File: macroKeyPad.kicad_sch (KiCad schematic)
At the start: 0 parts

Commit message: added libraries
Almost done, gotta add graphic and possibly change the thing for the kb2040
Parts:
- added D1, D2, D3, D4, D5, D6, D7, D8: Diode, ScottoKeebs_Components:Diode_SOD-123, symbol ScottoKeebs:Placeholder_Diode
- added S1, S2, S3, S4, S5, S6, S7, S8: Keyswitch, PCM_Switch_Keyboard_Kailh:SW_Kailh_Choc_V1, symbol ScottoKeebs:Placeholder_Keyswitch
- added U1: kb2040, ScottoKeebs_MCU:Adafruit_KB2040_SMD, symbol kb2040_kicad:kb2040
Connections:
- new net: D5.2 (A), S5.2
- new net: D4.2 (A), S4.2
- new net: D1.2 (A), S1.2
- new net: D6.2 (A), S6.2
- new net: D2.2 (A), S2.2
- new net: D3.2 (A), S3.2
- new net: D8.2 (A), S8.2
- new net: D7.2 (A), S7.2
- new net Col0: S1.1, S5.1, U1.19 (A3/29)
- new net Col1: S2.1, S6.1, U1.20 (A2/28)
- new net Col2: S3.1, S7.1, U1.21 (A1/27)
- new net Col3: S4.1, S8.1, U1.22 (A0/26)
- new net Row0: D1.1 (K), D2.1 (K), D3.1 (K), D4.1 (K), U1.23 (SCK/18)
- new net Row1: D5.1 (K), D6.1 (K), D7.1 (K), D8.1 (K), U1.24 (MISO/20)

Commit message: pretty close to being done
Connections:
- net Col0: now also U1.11 (D7); no longer U1.19 (A3/29)
- net Col1: now also U1.10 (D6); no longer U1.20 (A2/28)
- net Col2: now also U1.9 (D5); no longer U1.21 (A1/27)
- net Col3: now also U1.8 (D4); no longer U1.22 (A0/26)
- net Row0: now also U1.7 (D3); no longer U1.23 (SCK/18)
- net Row1: now also U1.6 (D2); no longer U1.24 (MISO/20)

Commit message: wiring
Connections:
- net Col0: no longer U1.11 (D7)
- net Col1: no longer U1.10 (D6)
- net Col2: no longer U1.9 (D5)
- net Col3: no longer U1.8 (D4)
- net Row0: no longer U1.7 (D3)
- net Row1: no longer U1.6 (D2)
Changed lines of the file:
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@@
-	(wire
-		(pts
-			(xy 59.69 74.93) (xy 57.15 74.93)
-		)
-		(stroke
-			(width 0)
-			(type default)
-		)
-	)
-	(wire
-		(pts
-			(xy 59.69 67.31) (xy 57.15 67.31)
-		)
-		(stroke
-			(width 0)
-			(type default)
-		)
-	)
-	(wire
-		(pts
-			(xy 59.69 69.85) (xy 57.15 69.85)
-		)
-		(stroke
-			(width 0)
-			(type default)
-		)
-	)
-	(wire
-		(pts
-			(xy 59.69 77.47) (xy 57.15 77.47)
-		)
-		(stroke
-			(width 0)
-			(type default)
-		)
-	)
 	(wire
 		(pts
@@
 	(wire
 		(pts
-			(xy 59.69 64.77) (xy 57.15 64.77)
-		)
-		(stroke
-			(width 0)
-			(type default)
-		)
-	)
-	(wire
-		(pts
 			(xy 149.86 85.09) (xy 160.02 85.09)
 		)
@@
 	(wire
 		(pts
-			(xy 59.69 72.39) (xy 57.15 72.39)
-		)
-		(stroke
-			(width 0)
-			(type default)
-		)
-	)
-	(wire
-		(pts
 			(xy 133.35 63.5) (xy 149.86 63.5)
 		)
@@
 	(global_label "Col3"
 		(shape input)
-		(at 57.15 69.85 180)
-		(fields_autoplaced yes)
-		(effects
-			(font
-				(size 1.27 1.27)
-			)
-			(justify right)
-		)
-		(property "Intersheetrefs" "${INTERSHEET_REFS}"
-			(at 49.8711 69.85 0)
+		(at 49.53 69.85 180)
+		(fields_autoplaced yes)
+		(effects
+			(font
+				(size 1.27 1.27)
+			)
+			(justify right)
+		)
+		(property "Intersheetrefs" "${INTERSHEET_REFS}"
+			(at 42.2511 69.85 0)
 			(effects
 				(font
@@
 	(global_label "Col0"
 		(shape input)
-		(at 57.15 77.47 180)
-		(fields_autoplaced yes)
-		(effects
-			(font
-				(size 1.27 1.27)
-			)
-			(justify right)
-		)
-		(property "Intersheetrefs" "${INTERSHEET_REFS}"
-			(at 49.8711 77.47 0)
+		(at 49.53 77.47 180)
+		(fields_autoplaced yes)
+		(effects
+			(font
+				(size 1.27 1.27)
+			)
+			(justify right)
+		)
+		(property "Intersheetrefs" "${INTERSHEET_REFS}"
+			(at 42.2511 77.47 0)
 			(effects
 				(font
@@
 	(global_label "Row1"
 		(shape input)
-		(at 57.15 64.77 180)
-		(fields_autoplaced yes)
-		(effects
-			(font
-				(size 1.27 1.27)
-			)
-			(justify right)
-		)
-		(property "Intersheetrefs" "${INTERSHEET_REFS}"
-			(at 49.2058 64.77 0)
+		(at 49.53 64.77 180)
+		(fields_autoplaced yes)
+		(effects
+			(font
+				(size 1.27 1.27)
+			)
+			(justify right)
+		)
+		(property "Intersheetrefs" "${INTERSHEET_REFS}"
+			(at 41.5858 64.77 0)
 			(effects
 				(font
@@
 	(global_label "Col1"
 		(shape input)
-		(at 57.15 74.93 180)
-		(fields_autoplaced yes)
-		(effects
-			(font
-				(size 1.27 1.27)
-			)
-			(justify right)
-		)
-		(property "Intersheetrefs" "${INTERSHEET_REFS}"
-			(at 49.8711 74.93 0)
+		(at 49.53 74.93 180)
+		(fields_autoplaced yes)
+		(effects
+			(font
+				(size 1.27 1.27)
+			)
+			(justify right)
+		)
+		(property "Intersheetrefs" "${INTERSHEET_REFS}"
+			(at 42.2511 74.93 0)
 			(effects
 				(font
@@
 	(global_label "Col2"
 		(shape input)
-		(at 57.15 72.39 180)
-		(fields_autoplaced yes)
-		(effects
-			(font
-				(size 1.27 1.27)
-			)
-			(justify right)
-		)
-		(property "Intersheetrefs" "${INTERSHEET_REFS}"
-			(at 49.8711 72.39 0)
+		(at 49.53 72.39 180)
+		(fields_autoplaced yes)
+		(effects
+			(font
+				(size 1.27 1.27)
+			)
+			(justify right)
+		)
+		(property "Intersheetrefs" "${INTERSHEET_REFS}"
+			(at 42.2511 72.39 0)
 			(effects
 				(font
@@
 	(global_label "Row0"
 		(shape input)
-		(at 57.15 67.31 180)
-		(fields_autoplaced yes)
-		(effects
-			(font
-				(size 1.27 1.27)
-			)
-			(justify right)
-		)
-		(property "Intersheetrefs" "${INTERSHEET_REFS}"
-			(at 49.2058 67.31 0)
-			(effects
-				(font
+		(at 49.53 67.31 180)
+		(fields_autoplaced yes)
+		(effects
+			(font
+				(size 1.27 1.27)
+			)
+			(justify right)
+		)
+		(property "Intersheetrefs" "${INTERSHEET_REFS}"
+			(at 41.5858 67.31 0)
+			(effects
+				(font

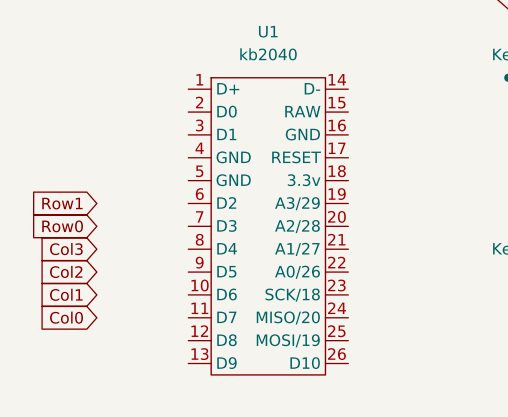
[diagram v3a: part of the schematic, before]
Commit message: added image and routes
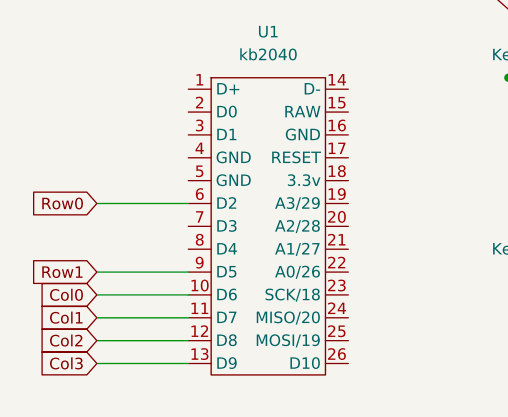
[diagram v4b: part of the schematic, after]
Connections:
- net Col0: now also U1.10 (D6)
- net Col1: now also U1.11 (D7)
- net Col2: now also U1.12 (D8)
- net Col3: now also U1.13 (D9)
- net Row0: now also U1.6 (D2)
- net Row1: now also U1.9 (D5)
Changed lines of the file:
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@@
+	(wire
+		(pts
+			(xy 49.53 72.39) (xy 59.69 72.39)
+		)
+		(stroke
+			(width 0)
+			(type default)
+		)
+	)
+	(wire
+		(pts
+			(xy 49.53 82.55) (xy 59.69 82.55)
+		)
+		(stroke
+			(width 0)
+			(type default)
+		)
+	)
+	(wire
+		(pts
+			(xy 49.53 74.93) (xy 59.69 74.93)
+		)
+		(stroke
+			(width 0)
+			(type default)
+		)
+	)
+	(wire
+		(pts
+			(xy 49.53 80.01) (xy 59.69 80.01)
+		)
+		(stroke
+			(width 0)
+			(type default)
+		)
+	)
 	(wire
 		(pts
@@
 	(wire
 		(pts
+			(xy 49.53 64.77) (xy 59.69 64.77)
+		)
+		(stroke
+			(width 0)
+			(type default)
+		)
+	)
+	(wire
+		(pts
 			(xy 144.78 43.18) (xy 144.78 50.8)
 		)
@@
 	(wire
 		(pts
+			(xy 49.53 77.47) (xy 59.69 77.47)
+		)
+		(stroke
+			(width 0)
+			(type default)
+		)
+	)
+	(wire
+		(pts
 			(xy 111.76 50.8) (xy 111.76 72.39)
 		)
@@
 	(global_label "Col3"
 		(shape input)
-		(at 49.53 69.85 180)
-		(fields_autoplaced yes)
-		(effects
-			(font
-				(size 1.27 1.27)
-			)
-			(justify right)
-		)
-		(property "Intersheetrefs" "${INTERSHEET_REFS}"
-			(at 42.2511 69.85 0)
+		(at 49.53 82.55 180)
+		(fields_autoplaced yes)
+		(effects
+			(font
+				(size 1.27 1.27)
+			)
+			(justify right)
+		)
+		(property "Intersheetrefs" "${INTERSHEET_REFS}"
+			(at 42.2511 82.55 0)
 			(effects
 				(font
@@
 	(global_label "Col0"
 		(shape input)
+		(at 49.53 74.93 180)
+		(fields_autoplaced yes)
+		(effects
+			(font
+				(size 1.27 1.27)
+			)
+			(justify right)
+		)
+		(property "Intersheetrefs" "${INTERSHEET_REFS}"
+			(at 42.2511 74.93 0)
+			(effects
+				(font
+					(size 1.27 1.27)
+				)
+				(justify right)
+				(hide yes)
+			)
+		)
+	)
+	(global_label "Row1"
+		(shape input)
+		(at 49.53 72.39 180)
+		(fields_autoplaced yes)
+		(effects
+			(font
+				(size 1.27 1.27)
+			)
+			(justify right)
+		)
+		(property "Intersheetrefs" "${INTERSHEET_REFS}"
+			(at 41.5858 72.39 0)
+			(effects
+				(font
+					(size 1.27 1.27)
+				)
+				(justify right)
+				(hide yes)
+			)
+		)
+	)
+	(global_label "Col1"
+		(shape input)
 		(at 49.53 77.47 180)
 		(fields_autoplaced yes)
@@
 		)
 	)
-	(global_label "Row1"
+	(global_label "Col2"
+		(shape input)
+		(at 49.53 80.01 180)
+		(fields_autoplaced yes)
+		(effects
+			(font
+				(size 1.27 1.27)
+			)
+			(justify right)
+		)
+		(property "Intersheetrefs" "${INTERSHEET_REFS}"
+			(at 42.2511 80.01 0)
+			(effects
+				(font
+					(size 1.27 1.27)
+				)
+				(justify right)
+				(hide yes)
+			)
+		)
+	)
+	(global_label "Col1"
+		(shape input)
+		(at 111.76 43.18 90)
+		(fields_autoplaced yes)
+		(effects
+			(font
+				(size 1.27 1.27)
+			)
+			(justify left)
+		)
+		(property "Intersheetrefs" "${INTERSHEET_REFS}"
+			(at 111.76 35.9011 90)
+			(effects
+				(font
+					(size 1.27 1.27)
+				)
+				(justify left)
+				(hide yes)
+			)
+		)
+	)
+	(global_label "Row0"
 		(shape input)
 		(at 49.53 64.77 180)
@@
 			(effects
 				(font
-					(size 1.27 1.27)
-				)
-				(justify right)
-				(hide yes)
-			)
-		)
-	)
-	(global_label "Col1"
-		(shape input)
-		(at 49.53 74.93 180)
-		(fields_autoplaced yes)
-		(effects
-			(font
-				(size 1.27 1.27)
-			)
-			(justify right)
-		)
-		(property "Intersheetrefs" "${INTERSHEET_REFS}"
-			(at 42.2511 74.93 0)
-			(effects
-				(font
-					(size 1.27 1.27)
-				)
-				(justify right)
-				(hide yes)
-			)
-		)
-	)
-	(global_label "Col2"
-		(shape input)
-		(at 49.53 72.39 180)
-		(fields_autoplaced yes)
-		(effects
-			(font
-				(size 1.27 1.27)
-			)
-			(justify right)
-		)
-		(property "Intersheetrefs" "${INTERSHEET_REFS}"
-			(at 42.2511 72.39 0)
-			(effects
-				(font
-					(size 1.27 1.27)
-				)
-				(justify right)
-				(hide yes)
-			)
-		)
-	)
-	(global_label "Col1"
-		(shape input)
-		(at 111.76 43.18 90)
-		(fields_autoplaced yes)
-		(effects
-			(font
-				(size 1.27 1.27)
-			)
-			(justify left)
-		)
-		(property "Intersheetrefs" "${INTERSHEET_REFS}"
-			(at 111.76 35.9011 90)
-			(effects
-				(font
-					(size 1.27 1.27)
-				)
-				(justify left)
-				(hide yes)
-			)
-		)
-	)
-	(global_label "Row0"
-		(shape input)
-		(at 49.53 67.31 180)
-		(fields_autoplaced yes)
-		(effects
-			(font
-				(size 1.27 1.27)
-			)
-			(justify right)
-		)
-		(property "Intersheetrefs" "${INTERSHEET_REFS}"
-			(at 41.5858 67.31 0)
-			(effects
-				(font
